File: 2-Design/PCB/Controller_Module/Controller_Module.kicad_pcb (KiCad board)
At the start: 2 copper layers, 200 x 50 mm, 13 parts, among them J1 Headers_GD1, J2 Headers_GD2, J3 Headers_GD3, J4 Headers_GD4, J5 Headers_GD5, J6 Headers_GD6, J7 Header_I_sense

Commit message: Some changes i dont even remember
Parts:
- SW_Gen_mode1, SW_Soft_st1: footprint Button_Switch_SMD:SW_Push_1P1T_NO_6x6mm_H9.5mm -> Button_Switch_THT:SW_PUSH_6mm_H8mm
- moved J1 20.0 mm to (221.2, 35.0)
- moved J2 20.0 mm to (191.2, 35.0)
- moved J3 20.0 mm to (161.2, 35.0)
- moved J4 20.0 mm to (131.2, 35.0)
- moved J5 20.0 mm to (101.2, 35.0)
- moved J6 20.0 mm to (71.2, 35.0)
- moved J7 15.1 mm to (247.5, 35.0)
- moved C1 10.3 mm to (234.0, 56.6)
- moved Pot_I_Set1 10.3 mm to (217.5, 74.5)
- moved R1 10.3 mm to (222.8, 55.0)
- moved STM32F103C8T1 4.03 mm to (114.7, 57.1)
- moved SW_Soft_st1 0.62 mm to (180.0, 70.0), turned to 180 degrees
- moved SW_Gen_mode1 0.62 mm to (191.1, 70.0), turned to 180 degrees
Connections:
- STM32F103C8T1 pad 25: Q6_PWM -> Q5_PWM
- STM32F103C8T1 pad 26: Q5_PWM -> Q6_PWM
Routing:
- net I_set: track 0.00 -> 125.6 mm
- net Q5_PWM: track 0.00 -> 75.2 mm
- net Q6_PWM: track 0.00 -> 70.9 mm
- net Soft_st: track 0.00 -> 60.2 mm
- net Net-(Pot_I_Set1-Pad2): track 0.00 -> 9.46 mm
- net I_sense: track 0.00 -> 2.16 mm
- net Q4_PWM: track 0.00 -> 2.11 mm
- net Q3_PWM: track 0.00 -> 2.11 mm
- net Q2_PWM: track 0.00 -> 2.11 mm
- net Q1_PWM: track 0.00 -> 2.11 mm
- added copper zone on B.Cu, net +5V
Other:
- board size 200 x 50 mm -> 230 x 50 mm

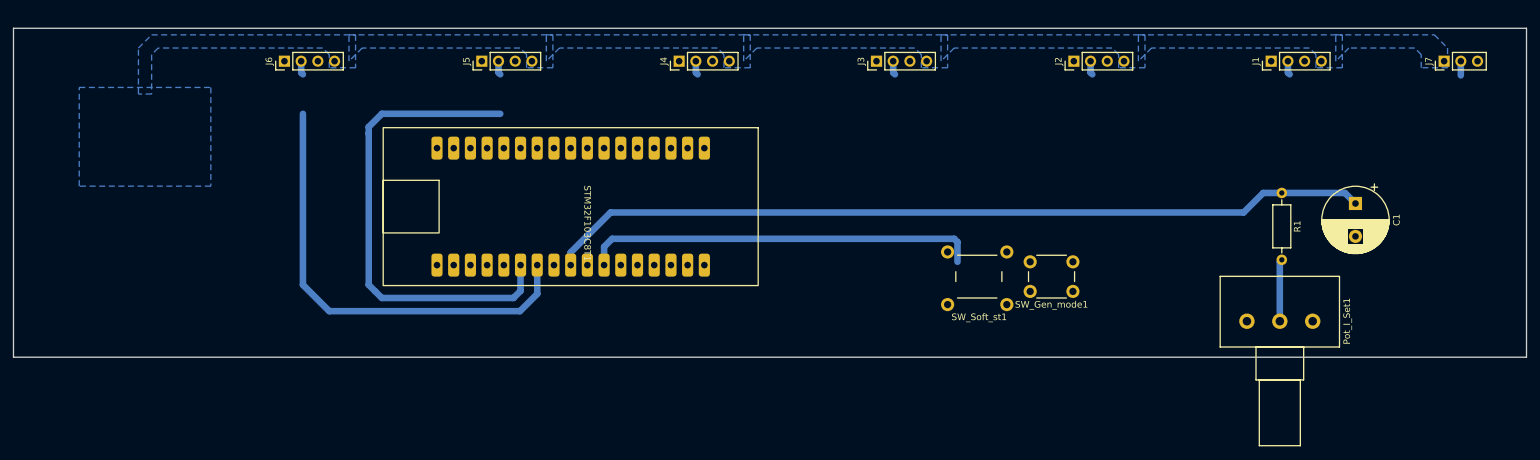
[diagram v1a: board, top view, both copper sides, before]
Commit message: Controller Module Completed
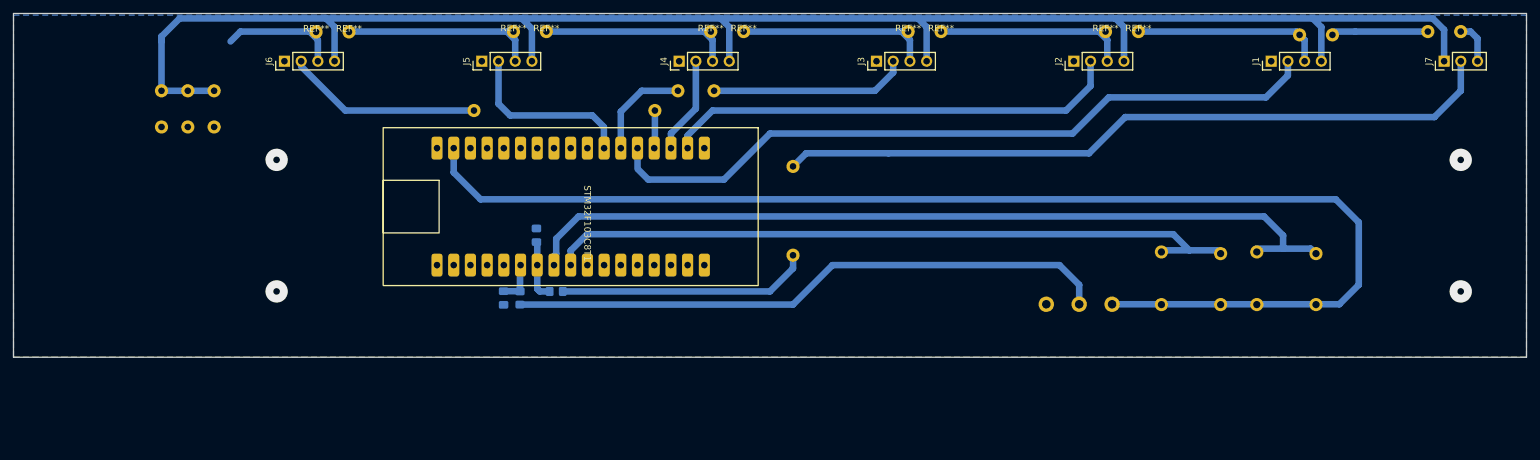
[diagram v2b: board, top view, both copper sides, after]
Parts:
- added ?: , , F.Cu at (230.5, 31.0)
- added ?: , , F.Cu at (52.5, 45.0)
- added ?: , , F.Cu at (196.0, 30.5)
- added ?: , , F.Cu at (60.5, 45.0)
- added ?: , , F.Cu at (100.0, 42.5)
- added ?: , , F.Cu at (136.5, 39.5)
- added ?: , , F.Cu at (52.5, 39.5)
- added ?: , , F.Cu at (127.5, 42.5)
- added ?: , , F.Cu at (148.5, 51.0)
- added ?: , , F.Cu at (106.0, 30.5)
- added ?: , , F.Cu at (166.0, 30.5)
- added ?: , , F.Cu at (56.5, 45.0)
- added ?: , , F.Cu at (60.5, 39.5)
- added ?: , , F.Cu at (250.0, 30.5)
- added ?: , , F.Cu at (136.0, 30.5)
- added ?: , , F.Cu at (225.5, 31.0)
- added ?: , , F.Cu at (131.0, 39.5)
- added ?: , , F.Cu at (148.5, 64.5)
- added ?: , , F.Cu at (56.5, 39.5)
- added ?: , , F.Cu at (245.0, 30.5)
- added C2: 100nF, Capacitor_SMD:C_0805_2012Metric_Pad1.18x1.45mm_HandSolder, B.Cu at (109.5, 61.5)
- added R2: 270R, Resistor_SMD:R_0805_2012Metric_Pad1.20x1.40mm_HandSolder, B.Cu at (112.5, 70.0)
- added REF**: Jumper_Wire_Hole, ee463_footprint_lib:Jumper_Wire_Hole, F.Cu at (201.0, 30.5)
- added REF**: Jumper_Wire_Hole, ee463_footprint_lib:Jumper_Wire_Hole, F.Cu at (111.0, 30.5)
- added REF**: Jumper_Wire_Hole, ee463_footprint_lib:Jumper_Wire_Hole, F.Cu at (81.0, 30.6)
- added REF**: Jumper_Wire_Hole, ee463_footprint_lib:Jumper_Wire_Hole, F.Cu at (171.0, 30.5)
- added REF**: Jumper_Wire_Hole, ee463_footprint_lib:Jumper_Wire_Hole, F.Cu at (141.0, 30.5)
- added REF**: Jumper_Wire_Hole, ee463_footprint_lib:Jumper_Wire_Hole, F.Cu at (76.0, 30.6)
- C1: value 4.7uF -> 100nF; footprint Capacitor_THT:CP_Radial_D10.0mm_P5.00mm -> Capacitor_SMD:C_0805_2012Metric_Pad1.18x1.45mm_HandSolder; moved to B.Cu
- Pot_I_Set1: value 100kR -> 33kR; moved to B.Cu
- R1: value 10kR -> 33kR; footprint Resistor_THT:R_Axial_DIN0207_L6.3mm_D2.5mm_P10.16mm_Horizontal -> Resistor_SMD:R_0805_2012Metric_Pad1.20x1.40mm_HandSolder; moved to B.Cu
- SW_Gen_mode1, SW_Soft_st1: moved to B.Cu
- moved C1 130.3 mm to (104.5, 71.0)
- moved R1 116.9 mm to (107.0, 71.0)
- moved SW_Soft_st1 40.0 mm to (220.0, 70.0), turned to 0 degrees
- moved Pot_I_Set1 20.7 mm to (197.0, 72.0)
- moved SW_Gen_mode1 18.1 mm to (209.0, 67.8), turned to 0 degrees
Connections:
- J7 pad 2: I_sense -> Net-(J7-Pad2)
- STM32F103C8T1 pad 2: unconnected-(STM32F103C8T1-Pad2) -> Q2_PWM
- STM32F103C8T1 pad 25: Q5_PWM -> I_set
- STM32F103C8T1 pad 26: Q6_PWM -> I_sense
- STM32F103C8T1 pad 27: I_sense -> Soft_st
- STM32F103C8T1 pad 28: I_set -> Gen_mode
- STM32F103C8T1 pad 29: Gen_mode -> GPIO_IN_D
- STM32F103C8T1 pad 3: unconnected-(STM32F103C8T1-Pad3) -> Q4_PWM
- STM32F103C8T1 pad 30: Soft_st -> GPIO_OUT_D
- STM32F103C8T1 pad 31: V_sense -> unconnected-(STM32F103C8T1-Pad31)
- STM32F103C8T1 pad 32: GPIO_INPUT_D -> unconnected-(STM32F103C8T1-Pad32)
- STM32F103C8T1 pad 4: unconnected-(STM32F103C8T1-Pad4) -> Q6_PWM
- STM32F103C8T1 pad 6: Q2_PWM -> Q3_PWM
- STM32F103C8T1 pad 7: Q3_PWM -> Q5_PWM
- STM32F103C8T1 pad 8: Q4_PWM -> unconnected-(STM32F103C8T1-Pad8)
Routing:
- net +5V: track 0.00 -> 260.5 mm
- net +3V3: track 0.00 -> 192.9 mm
- net GND: track 0.00 -> 183.9 mm
- net Net-(J7-Pad2): track 0.00 -> 149.7 mm
- net I_set: track 125.6 -> 6.80 mm
- net Q1_PWM: track 2.11 -> 111.2 mm
- net Gen_mode: track 0.00 -> 107.8 mm
- net Net-(Pot_I_Set1-Pad2): track 9.46 -> 91.7 mm
- net Soft_st: track 60.2 -> 128.6 mm
- net Q2_PWM: track 2.11 -> 70.1 mm
- net Q5_PWM: track 75.2 -> 27.2 mm
- net Q3_PWM: track 2.11 -> 46.1 mm
- net Q6_PWM: track 70.9 -> 35.6 mm
- net Q4_PWM: track 2.11 -> 14.8 mm
- net I_sense: track 2.16 -> 8.71 mm
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- added copper zone on B.Cu, net GND
- removed copper zone on B.Cu, net +5V
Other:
- board size 230 x 50 mm -> 230 x 52.2 mm
- board text added: "Jumper_Wire_Hole"
- board text added: "REF**"
